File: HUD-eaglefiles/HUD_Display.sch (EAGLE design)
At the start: 3 parts

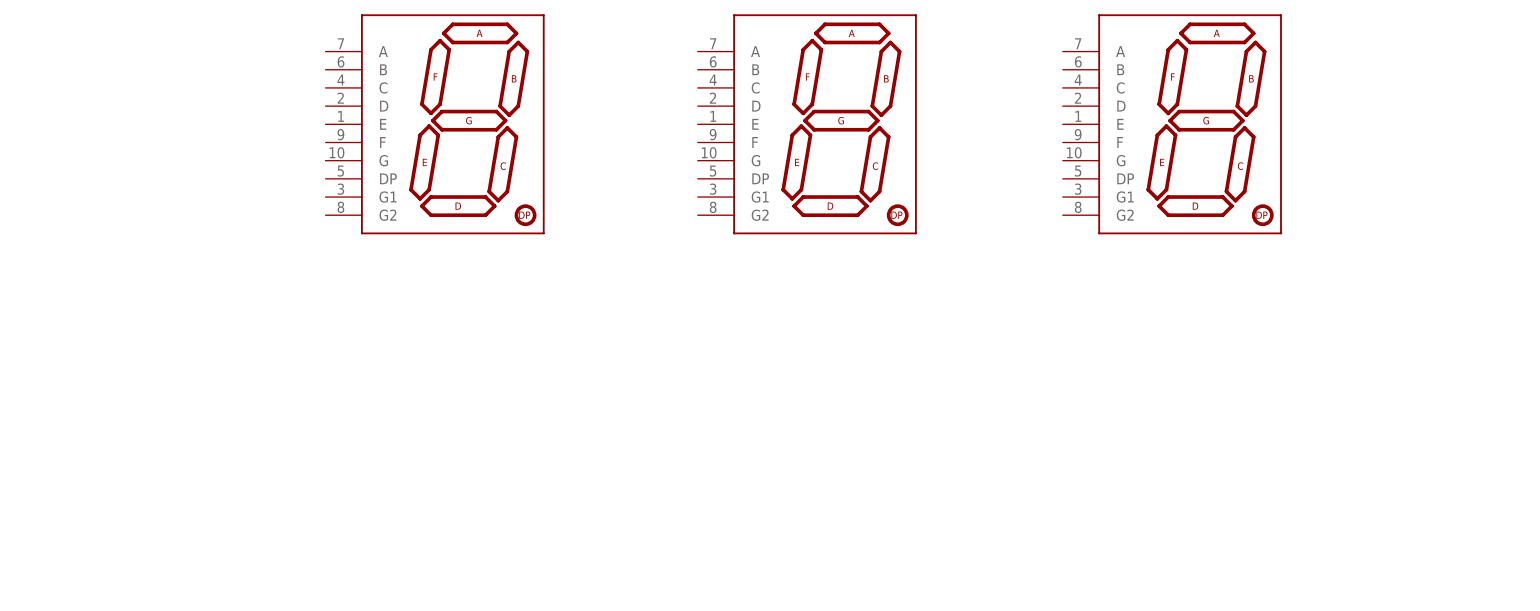
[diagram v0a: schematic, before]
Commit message: created initial connections for display
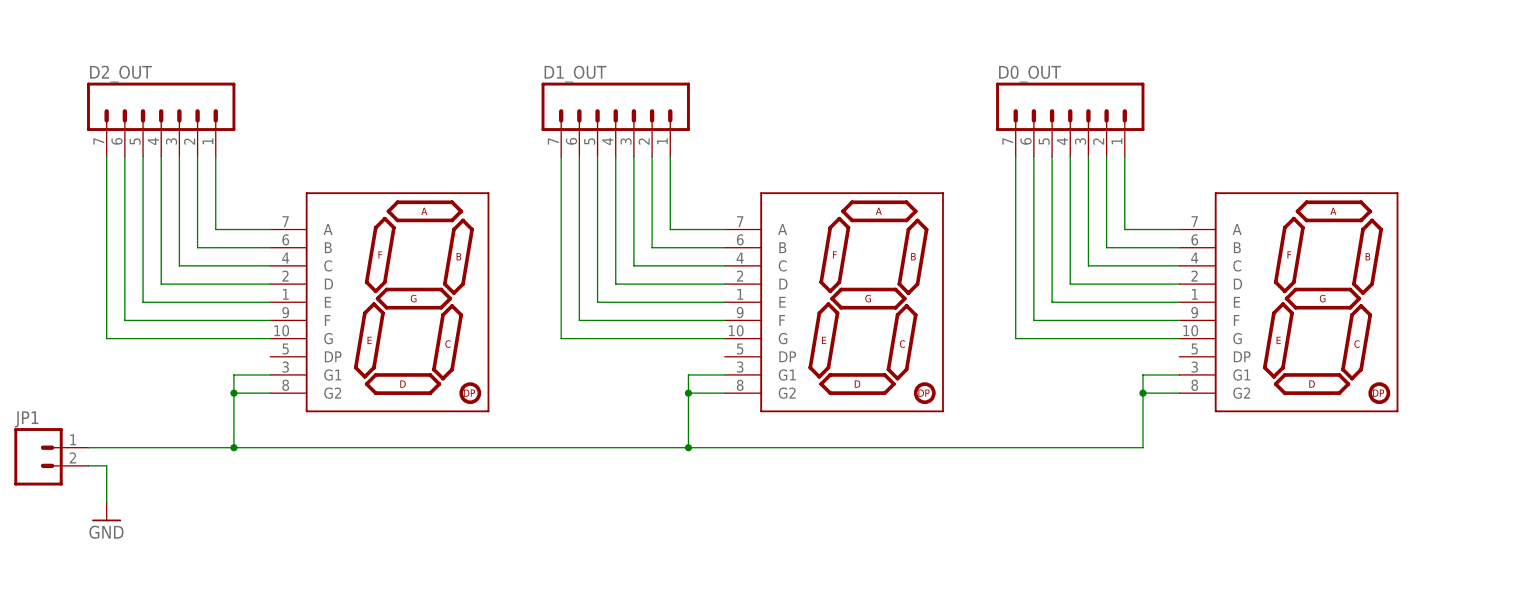
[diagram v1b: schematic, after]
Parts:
- removed U$1, U$2, U$3: 7-SEGMENT-DISPLAY-1"-REDEZ, SparkFun-Displays:7-SEGMENT-DISPLAY-1"-REDEZ
- added D0, D1, D2: 7-SEGMENT-DISPLAY-1"-REDEZ, SparkFun-Displays:7-SEGMENT-DISPLAY-1"-REDEZ
- added D0_OUT, D1_OUT, D2_OUT: (no value), SparkFun-Connectors:M07
- added JP1: (no value), SparkFun-Connectors:M02PTH
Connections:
- new net D1_OUT: D1.F, D1_OUT.6
- new net DO_OUT: D2.G, D2_OUT.7
- new net GND: JP1.2
- new net N$1: D2.A, D2_OUT.1
- new net N$10: D1.C, D1_OUT.3
- new net N$11: D1.D, D1_OUT.4
- new net N$12: D1.E, D1_OUT.5
- new net N$14: D1.G, D1_OUT.7
- new net N$15: D0.A, D0_OUT.1
- new net N$16: D0.B, D0_OUT.2
- new net N$17: D0.C, D0_OUT.3
- new net N$18: D0.D, D0_OUT.4
- new net N$19: D0.E, D0_OUT.5
- new net N$2: D2.B, D2_OUT.2
- new net N$20: D0.F, D0_OUT.6
- new net N$21: D0.G, D0_OUT.7
- new net N$3: D2.C, D2_OUT.3
- new net N$4: D2.D, D2_OUT.4
- new net N$5: D2.E, D2_OUT.5
- new net N$6: D2.F, D2_OUT.6
- new net N$8: D1.A, D1_OUT.1
- new net N$9: D1.B, D1_OUT.2
- new net VCC: D0.G1, D0.G2, D1.G1, D1.G2, D2.G1, D2.G2, JP1.1

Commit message: finilised display cicuit schematic
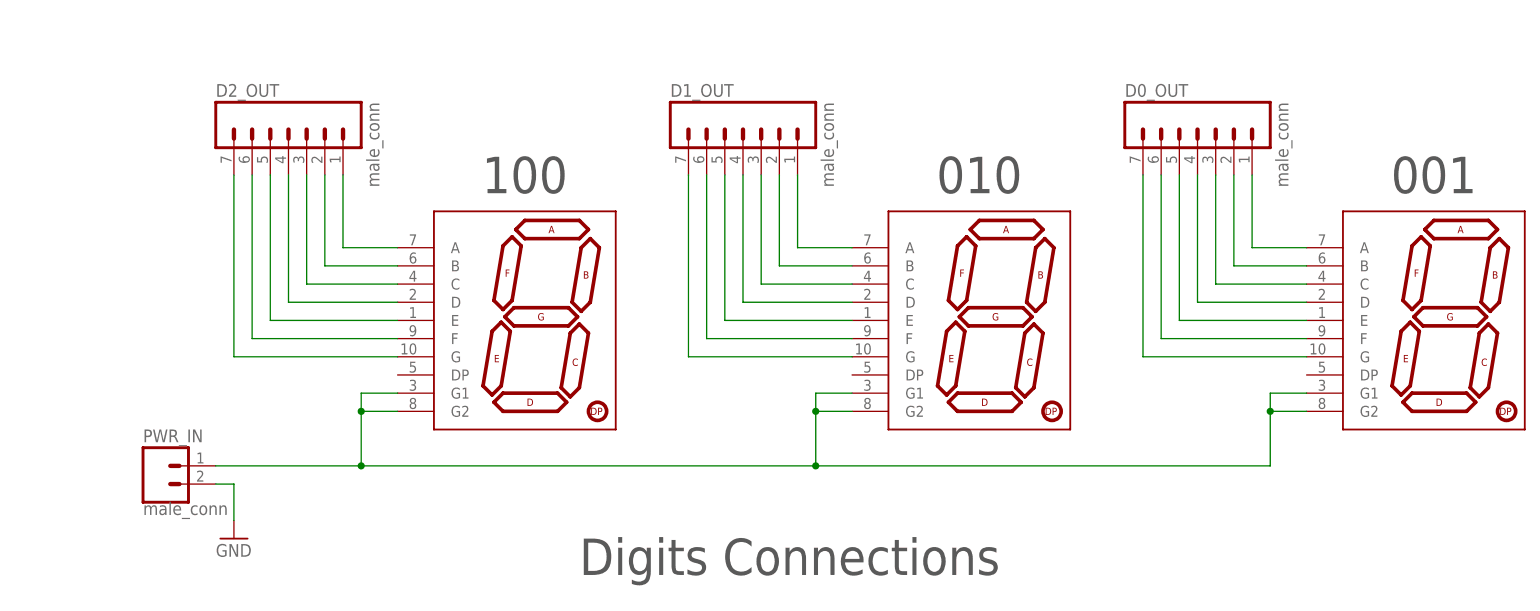
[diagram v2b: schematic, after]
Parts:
- removed JP1: (no value), SparkFun-Connectors:M02PTH
- added PWR_IN: male_conn, SparkFun-Connectors:M02PTH
- D0_OUT, D1_OUT, D2_OUT: value (none) -> male_conn
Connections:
- net GND: now also PWR_IN.2; no longer JP1.2
- net VCC: now also PWR_IN.1; no longer JP1.1
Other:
- note added: "001"
- note added: "010"
- note added: "100"
- note added: "Digits Connections"
- note added: "These digits are not going to be soldered on the PCB directly. Instead female headers are"
- note added: "parts replicable in case they were burnt."
- note added: "soldered on the PCB and the 7-segments are pluged into them. This is meant to make the"
- moved on the sheet: D0_OUT, D1_OUT, D2_OUT
